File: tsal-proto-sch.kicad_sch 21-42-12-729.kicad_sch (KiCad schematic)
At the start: 29 parts, among them J1 043045-0412, Q1 DMP2035U-7, Q3 UJ3N065080K3S, Q4 DMN2056U, Q5 AO3401A, U1 H11L1M, U2 NE555D

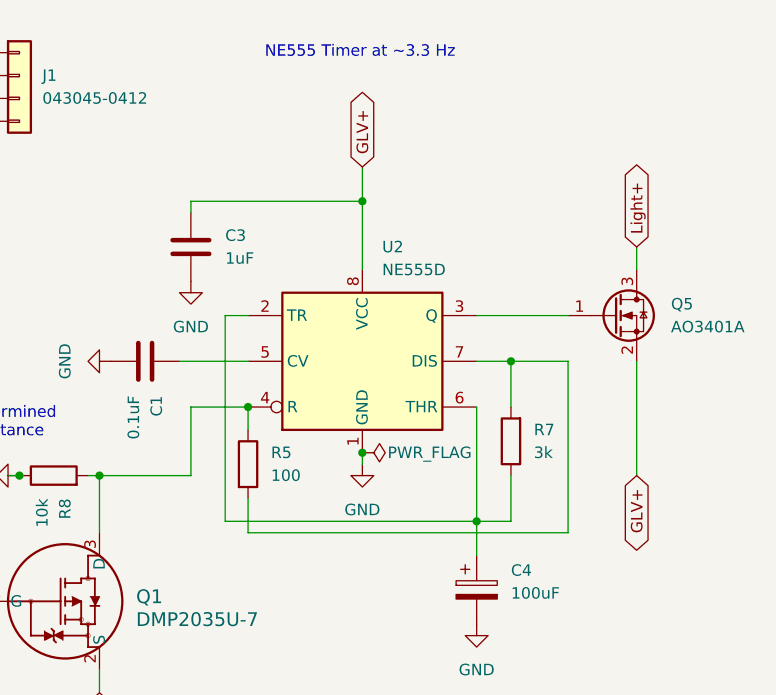
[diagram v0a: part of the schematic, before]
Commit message: netlist for pcb added
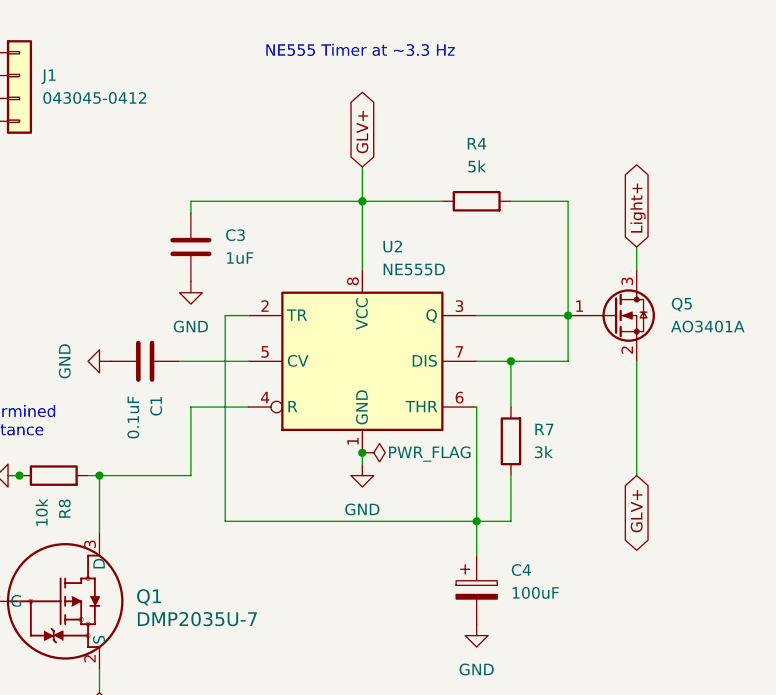
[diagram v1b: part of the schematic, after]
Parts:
- removed R5: 100, Resistor_SMD:R_0805_2012Metric_Pad1.20x1.40mm_HandSolder, symbol Device:R
- added R4: 5k, symbol Device:R
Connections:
- net GLV+: now also R4.1
- net at Q5.1 (G), U2.3 (Q): now also R7.2, U2.7 (DIS), R4.2
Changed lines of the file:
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@@
+	)
+	(junction
+		(at 176.53 54.61)
+		(diameter 0)
+		(color 0 0 0 0)
 	)
 	(junction
@@
 	)
 	(junction
-		(at 140.97 64.77)
-		(diameter 0)
-		(color 0 0 0 0)
-	)
-	(junction
 		(at 153.67 69.85)
 		(diameter 0)
@@
 	(wire
 		(pts
-			(xy 140.97 74.93) (xy 140.97 78.74)
-		)
-		(stroke
-			(width 0)
-			(type default)
-		)
-	)
-	(wire
-		(pts
 			(xy 133.35 59.69) (xy 140.97 59.69)
 		)
@@
 	(wire
 		(pts
-			(xy 176.53 78.74) (xy 140.97 78.74)
-		)
-		(stroke
-			(width 0)
-			(type default)
-		)
-	)
-	(wire
-		(pts
 			(xy 78.74 88.9) (xy 69.85 88.9)
 		)
@@
 	(wire
 		(pts
+			(xy 176.53 41.91) (xy 176.53 54.61)
+		)
+		(stroke
+			(width 0)
+			(type default)
+		)
+	)
+	(wire
+		(pts
 			(xy 86.36 68.58) (xy 102.87 68.58)
 		)
@@
 	(wire
 		(pts
+			(xy 176.53 54.61) (xy 176.53 59.69)
+		)
+		(stroke
+			(width 0)
+			(type default)
+		)
+	)
+	(wire
+		(pts
 			(xy 166.37 64.77) (xy 166.37 77.47)
 		)
@@
 	(wire
 		(pts
+			(xy 170.18 41.91) (xy 176.53 41.91)
+		)
+		(stroke
+			(width 0)
+			(type default)
+		)
+	)
+	(wire
+		(pts
 			(xy 166.37 77.47) (xy 138.43 77.47)
 		)
@@
 	(wire
 		(pts
-			(xy 140.97 64.77) (xy 140.97 67.31)
-		)
-		(stroke
-			(width 0)
-			(type default)
-		)
-	)
-	(wire
-		(pts
 			(xy 52.07 116.84) (xy 52.07 114.3)
 		)
@@
 	(wire
 		(pts
+			(xy 153.67 41.91) (xy 162.56 41.91)
+		)
+		(stroke
+			(width 0)
+			(type default)
+		)
+	)
+	(wire
+		(pts
 			(xy 93.98 27.94) (xy 110.49 27.94)
 		)
@@
 		(pts
 			(xy 102.87 68.58) (xy 102.87 71.12)
-		)
-		(stroke
-			(width 0)
-			(type default)
-		)
-	)
-	(wire
-		(pts
-			(xy 176.53 59.69) (xy 176.53 78.74)
 		)
 		(stroke
@@
 	(symbol
 		(lib_id "Device:R")
+		(at 166.37 41.91 90)
+		(unit 1)
+		(exclude_from_sim no)
+		(in_bom yes)
+		(on_board yes)
+		(dnp no)
+		(fields_autoplaced yes)
+		(property "Reference" "R4"
+			(at 166.37 35.56 90)
+			(effects
+				(font
+					(size 1.27 1.27)
+				)
+			)
+		)
+		(property "Value" "5k"
+			(at 166.37 38.1 90)
+			(effects
+				(font
+					(size 1.27 1.27)
+				)
+			)
+		)
+		(property "Footprint" ""
+			(at 166.37 43.688 90)
+			(effects
+				(font
+					(size 1.27 1.27)
+				)
+				(hide yes)
+			)
+		)
+		(property "Datasheet" "~"
+			(at 166.37 41.91 0)
+			(effects
+				(font
+					(size 1.27 1.27)
+				)
+				(hide yes)
+			)
+		)
+		(property "Description" "Resistor"
+			(at 166.37 41.91 0)
+			(effects
+				(font
+					(size 1.27 1.27)
+				)
+				(hide yes)
+			)
+		)
+		(pin "1"
+		)
+		(pin "2"
+		)
+		(instances
+			(project ""
+				(path "/d0262e13-a8ab-42db-962e-1ef7dd9c8d4a"
+					(reference "R4")
+					(unit 1)
+				)
+			)
+		)
+	)
+	(symbol
+		(lib_id "Device:R")
 		(at 52.07 93.98 0)
 		(unit 1)
@@
 					(unit 1)
 				)
-			)
-		)
-	)
-	(symbol
-		(lib_id "Device:R")
-		(at 140.97 71.12 0)
-		(unit 1)
-		(exclude_from_sim no)
-		(in_bom yes)
-		(on_board yes)
-		(dnp no)
-		(fields_autoplaced yes)
-		(property "Reference" "R5"
-			(at 143.51 69.8499 0)
-			(effects
-				(font
-					(size 1.27 1.27)
-				)
-				(justify left)
-			)
-		)
-		(property "Value" "100"
-			(at 143.51 72.3899 0)
-			(effects
-				(font
-					(size 1.27 1.27)
-				)
-				(justify left)
-			)
-		)
-		(property "Footprint" "Resistor_SMD:R_0805_2012Metric_Pad1.20x1.40mm_HandSolder"
-			(at 139.192 71.12 90)
-			(effects
-				(font
-					(size 1.27 1.27)
-				)
-				(hide yes)
-			)
-		)
-		(property "Datasheet" "~"
-			(at 140.97 71.12 0)
-			(effects
-				(font
-					(size 1.27 1.27)
-				)
-				(hide yes)
-			)
-		)
-		(property "Description" "Resistor"
-			(at 140.97 71.12 0)
-			(effects
-				(font
-					(size 1.27 1.27)
-				)
-				(hide yes)
-			)
-		)
-		(pin "2"
-		)
-		(pin "1"
-		)
-		(instances
-			(project "TSALv2"
-				(path "/d0262e13-a8ab-42db-962e-1ef7dd9c8d4a"
-					(reference "R5")
-					(unit 1)
-				)
